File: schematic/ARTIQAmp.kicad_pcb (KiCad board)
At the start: 2 copper layers, 297 parts, among them J1 Power conneciton, J2 HD68, J3 HD68, U1 OPA454AIDDAR, U10 OPA454AIDDAR, U11 OPA454AIDDAR, U12 OPA454AIDDAR, U13 OPA454AIDDAR, U14 OPA454AIDDAR, U15 OPA454AIDDAR, U16 OPA454AIDDAR, U17 OPA454AIDDAR, U18 OPA454AIDDAR, U19 OPA454AIDDAR, U2 OPA454AIDDAR, U20 OPA454AIDDAR, U21 OPA454AIDDAR, U22 OPA454AIDDAR, U23 OPA454AIDDAR, U24 OPA454AIDDAR, U25 OPA454AIDDAR, U26 OPA454AIDDAR, U27 OPA454AIDDAR, U28 OPA454AIDDAR, U29 OPA454AIDDAR, U3 OPA454AIDDAR, U30 OPA454AIDDAR, U31 OPA454AIDDAR, U32 OPA454AIDDAR, U4 OPA454AIDDAR, U5 OPA454AIDDAR, U6 OPA454AIDDAR, U7 OPA454AIDDAR, U8 OPA454AIDDAR, U9 OPA454AIDDAR

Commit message: Update libraries for new components
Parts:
- added FL1: NFE61PT472C1H9L, ARTIQAmp:NFE61, F.Cu at (178.5, 211.5)
- added FL10: NFE61PT472C1H9L, ARTIQAmp:NFE61, F.Cu at (261.0, 182.2)
- added FL11: NFE61PT472C1H9L, ARTIQAmp:NFE61, F.Cu at (223.8, 182.2)
- added FL12: NFE61PT472C1H9L, ARTIQAmp:NFE61, F.Cu at (207.6, 36.6)
- added FL13: NFE61PT472C1H9L, ARTIQAmp:NFE61, F.Cu at (243.5, 182.2)
- added FL14: NFE61PT472C1H9L, ARTIQAmp:NFE61, F.Cu at (368.3, 129.3)
- added FL15: NFE61PT472C1H9L, ARTIQAmp:NFE61, F.Cu at (279.5, 182.5)
- added FL16: NFE61PT472C1H9L, ARTIQAmp:NFE61, F.Cu at (207.6, 26.2)
- added FL17: NFE61PT472C1H9L, ARTIQAmp:NFE61, B.Cu at (163.8, 249.8)
- added FL18: NFE61PT472C1H9L, ARTIQAmp:NFE61, B.Cu at (183.5, 249.0)
- added FL19: NFE61PT472C1H9L, ARTIQAmp:NFE61, B.Cu at (125.8, 250.0)
- added FL2: NFE61PT472C1H9L, ARTIQAmp:NFE61, F.Cu at (379.3, 102.3)
- added FL20: NFE61PT472C1H9L, ARTIQAmp:NFE61, F.Cu at (-0.35, 228.0)
- added FL21: NFE61PT472C1H9L, ARTIQAmp:NFE61, B.Cu at (201.0, 249.0)
- added FL22: NFE61PT472C1H9L, ARTIQAmp:NFE61, F.Cu at (428.8, 215.2)
- added FL23: NFE61PT472C1H9L, ARTIQAmp:NFE61, F.Cu at (57.2, 105.2)
- added FL24: NFE61PT472C1H9L, ARTIQAmp:NFE61, B.Cu at (143.2, 250.0)
- added FL25: NFE61PT472C1H9L, ARTIQAmp:NFE61, F.Cu at (127.0, 145.8)
- added FL26: NFE61PT472C1H9L, ARTIQAmp:NFE61, F.Cu at (180.2, 181.5)
- added FL27: NFE61PT472C1H9L, ARTIQAmp:NFE61, F.Cu at (-0.35, 207.2)
- added FL28: NFE61PT472C1H9L, ARTIQAmp:NFE61, F.Cu at (200.2, 181.0)
- added FL29: NFE61PT472C1H9L, ARTIQAmp:NFE61, F.Cu at (162.8, 181.5)
- added FL3: NFE61PT472C1H9L, ARTIQAmp:NFE61, F.Cu at (220.1, 2.58)
- added FL30: NFE61PT472C1H9L, ARTIQAmp:NFE61, F.Cu at (-0.35, 196.8)
- added FL31: NFE61PT472C1H9L, ARTIQAmp:NFE61, F.Cu at (267.2, 145.8)
- added FL32: NFE61PT472C1H9L, ARTIQAmp:NFE61, F.Cu at (-0.35, 186.4)
- added FL4: NFE61PT472C1H9L, ARTIQAmp:NFE61, F.Cu at (161.0, 211.5)
- added FL5: NFE61PT472C1H9L, ARTIQAmp:NFE61, F.Cu at (408.4, 261.0)
- added FL6: NFE61PT472C1H9L, ARTIQAmp:NFE61, F.Cu at (143.5, 211.5)
- added FL7: NFE61PT472C1H9L, ARTIQAmp:NFE61, F.Cu at (207.6, 47.0)
- added FL8: NFE61PT472C1H9L, ARTIQAmp:NFE61, F.Cu at (284.1, 31.6)
- added FL9: NFE61PT472C1H9L, ARTIQAmp:NFE61, F.Cu at (220.1, -7.83)
- C100, C72, C76, C80, C88: value 0.27uF -> 5nF; moved to B.Cu
- C101, C73, C77, C81, C89: value 1.3nF -> 160p; moved to B.Cu
- C102, C71, C74, C75, C78, C79, C82, C87, C90, C99, R65, R67, R68, R69, R71, R72, R73, R75, R76, R81, R83, R84, R93, R95, R96, U17, U18, U19, U21, U24: moved to B.Cu
- C104, C108, C112, C116, C12, C120, C124, C128, C132, C16, C20, C24, C28, C32, C36, C40, C44, C48, C52, C56, C60, C64, C68, C8, C84, C92, C96: value 0.27uF -> 5nF
- C105, C109, C113, C117, C121, C125, C129, C13, C133, C17, C21, C25, C29, C33, C37, C41, C45, C49, C53, C57, C61, C65, C69, C85, C9, C93, C97: value 1.3nF -> 160p
- R10, R102, R106, R110, R114, R118, R122, R126, R14, R18, R2, R22, R26, R30, R34, R38, R42, R46, R50, R54, R58, R6, R62, R78, R86, R90, R98: value 49R9 -> 30R
- R66, R70, R74, R82, R94: value 49R9 -> 30R; moved to B.Cu
- moved C112 337.2 mm to (425.8, 201.6)
- moved C114 337.2 mm to (429.8, 201.6)
- moved C127 337.2 mm to (449.9, 201.6)
- moved C129 337.2 mm to (445.9, 201.6)
- moved C130 337.2 mm to (457.9, 200.0)
- moved C84 337.2 mm to (413.7, 188.9)
- moved C85 337.2 mm to (417.7, 187.4)
- moved C91 337.2 mm to (437.8, 187.4)
- moved C92 337.2 mm to (438.3, 184.9)
- moved C93 337.2 mm to (433.8, 188.9)
- moved C94 337.2 mm to (438.3, 182.4)
- moved C96 337.2 mm to (413.7, 201.6)
- moved C97 337.2 mm to (417.7, 200.0)
- moved R105 337.2 mm to (438.3, 195.0)
- moved R106 337.2 mm to (433.8, 201.6)
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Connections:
- R10 pad 2: /D4_IN -> Net-(FL3-Pad2)
- R102 pad 2: /D27_IN -> Net-(FL26-Pad2)
- R106 pad 2: /D28_IN -> Net-(FL27-Pad2)
- R110 pad 2: /D29_IN -> Net-(FL28-Pad2)
- R114 pad 2: /D30_IN -> Net-(FL29-Pad2)
- R118 pad 2: /D31_IN -> Net-(FL30-Pad2)
- R122 pad 2: /D32_IN -> Net-(FL31-Pad2)
- R126 pad 2: /D25_IN -> Net-(FL32-Pad2)
- R14 pad 2: /D5_IN -> Net-(FL4-Pad2)
- R18 pad 2: /D6_IN -> Net-(FL5-Pad2)
- R2 pad 2: /D2_IN -> Net-(FL1-Pad2)
- R22 pad 2: /D7_IN -> Net-(FL6-Pad2)
- R26 pad 2: /D8_IN -> Net-(FL7-Pad2)
- R30 pad 2: /D1_IN -> Net-(FL8-Pad2)
- R34 pad 2: /D10_IN -> Net-(FL9-Pad2)
- R38 pad 2: /D11_IN -> Net-(FL10-Pad2)
- R42 pad 2: /D12_IN -> Net-(FL11-Pad2)
- R46 pad 2: /D13_IN -> Net-(FL12-Pad2)
- R50 pad 2: /D14_IN -> Net-(FL13-Pad2)
- R54 pad 2: /D15_IN -> Net-(FL14-Pad2)
- R58 pad 2: /D16_IN -> Net-(FL15-Pad2)
- R6 pad 2: /D3_IN -> Net-(FL2-Pad2)
- R62 pad 2: /D9_IN -> Net-(FL16-Pad2)
- R66 pad 2: /D18_IN -> Net-(FL17-Pad2)
- R70 pad 2: /D19_IN -> Net-(FL18-Pad2)
- R74 pad 2: /D20_IN -> Net-(FL19-Pad2)
- R78 pad 2: /D21_IN -> Net-(FL20-Pad2)
- R82 pad 2: /D22_IN -> Net-(FL21-Pad2)
- R86 pad 2: /D23_IN -> Net-(FL22-Pad2)
- R90 pad 2: /D24_IN -> Net-(FL23-Pad2)
- R94 pad 2: /D17_IN -> Net-(FL24-Pad2)
- R98 pad 2: /D26_IN -> Net-(FL25-Pad2)
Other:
- board outline added: 380 x 160 mm
- copper layers 2 -> 8

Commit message: finalize schematic and start organizing components in layout
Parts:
- removed the C100 at (147.0, 256.2)
- removed the C101 at (149.8, 263.5)
- removed the C102 at (153.5, 254.2)
- removed C103, C106, C119, C122, C123: 0.1uF, Capacitor_SMD:C_0603_1608Metric
- removed C104, C120: 5nF, Capacitor_SMD:C_0603_1608Metric
- removed C105, C109, C113, C117, C121, C125, C129, C133: 160p, Capacitor_SMD:C_0603_1608Metric
- removed the C13 at (464.0, 239.1)
- removed the C17 at (471.8, 180.0)
- removed the C21 at (167.5, 198.0)
- removed the C25 at (443.2, 268.8)
- removed the C27 at (156.8, 204.2)
- removed the C33 at (471.8, 167.3)
- removed the C35 at (466.4, 261.9)
- removed the C36 at (461.8, 265.9)
- removed the C37 at (466.4, 259.4)
- removed the C38 at (470.4, 259.4)
- removed the C41 at (385.9, 184.8)
- removed the C45 at (267.5, 168.8)
- removed the C49 at (230.2, 168.8)
- removed the C53 at (471.3, 157.2)
- removed the C65 at (286.0, 169.0)
- removed the C71 at (177.0, 257.0)
- removed the C72 at (167.5, 256.0)
- removed the C73 at (170.2, 263.2)
- removed the C74 at (174.0, 254.0)
- removed the C75 at (196.8, 256.2)
- removed the C82 at (136.0, 254.2)
- removed the C85 at (417.7, 187.4)
- removed the C87 at (214.2, 256.2)
- removed the C88 at (204.8, 255.2)
- removed the C89 at (207.5, 262.5)
- removed the C9 at (185.0, 198.0)
- removed the C90 at (211.2, 253.2)
- removed the C97 at (417.7, 200.0)
- removed the C99 at (156.5, 257.2)
- removed the R116 at (165.2, 172.8)
- removed the R17 at (430.7, 272.8)
- removed the R23 at (150.0, 199.8)
- removed the R24 at (146.0, 202.8)
- removed the R29 at (457.8, 265.9)
- removed the R30 at (465.8, 265.9)
- removed the R41 at (236.0, 170.5)
- removed the R5 at (460.0, 236.6)
- removed the R53 at (389.9, 172.1)
- removed the R65 at (176.0, 261.5)
- removed the R66 at (165.0, 256.8)
- removed the R68 at (166.2, 258.5)
- removed the R71 at (190.0, 260.8)
- removed the R72 at (186.0, 257.8)
- removed the R74 at (127.0, 257.0)
- removed the R83 at (207.5, 260.8)
- removed the R84 at (203.5, 257.8)
- removed the R89 at (405.7, 201.6)
- removed the R95 at (149.8, 261.8)
- removed the R96 at (145.8, 258.8)
- removed U1, U10, U11, U12, U13, U14, U15, U16, U17, U18, U19, U2, U20, U21, U22, U23, U24, U25, U26, U27, U28, U29, U3, U30, U31, U32, U4, U5, U6, U7, U8, U9: OPA454AIDDAR, ARTIQAmp:TI_SO-PowerPAD-8_ThermalVias
- added C22: 0.1uF, Capacitor_SMD:C_0603_1608Metric, F.Cu at (224.8, 157.8)
- added C23: 1nF, Capacitor_SMD:C_0603_1608Metric, F.Cu at (215.6, 160.2)
- added C24: 0.1uF, Capacitor_SMD:C_0603_1608Metric, F.Cu at (222.4, 160.8)
- added C43: 0.1uF, Capacitor_SMD:C_0603_1608Metric, F.Cu at (224.8, 134.8)
- added C56: 1nF, Capacitor_SMD:C_0603_1608Metric, F.Cu at (153.5, 160.2)
- added C58: 0.1uF, Capacitor_SMD:C_0603_1608Metric, F.Cu at (183.4, 157.8)
- added C59: 1nF, Capacitor_SMD:C_0603_1608Metric, F.Cu at (174.2, 160.2)
- added C60: 0.1uF, Capacitor_SMD:C_0603_1608Metric, F.Cu at (181.0, 160.8)
- added C62: 1nF, Capacitor_SMD:C_0603_1608Metric, F.Cu at (112.1, 160.2)
- added C63: 0.1uF, Capacitor_SMD:C_0603_1608Metric, F.Cu at (118.9, 160.8)
- added C67: 0.1uF, Capacitor_SMD:C_0603_1608Metric, F.Cu at (204.1, 157.8)
- added C68: 1nF, Capacitor_SMD:C_0603_1608Metric, F.Cu at (194.9, 160.2)
- added C91: 0.1uF, Capacitor_SMD:C_0603_1608Metric, F.Cu at (142.0, 134.8)
- added C92: 1nF, Capacitor_SMD:C_0603_1608Metric, F.Cu at (132.8, 137.2)
- added C94: 0.1uF, Capacitor_SMD:C_0603_1608Metric, F.Cu at (286.9, 157.8)
- added IC1: LTC6090CS8E#PBF, ARTIQAmp:SOIC127P599X175-9N, F.Cu at (261.6, 157.2)
- added IC10: LTC6090CS8E#PBF, ARTIQAmp:SOIC127P599X175-9N, F.Cu at (240.9, 134.2)
- added IC11: LTC6090CS8E#PBF, ARTIQAmp:SOIC127P599X175-9N, F.Cu at (199.5, 134.2)
- added IC12: LTC6090CS8E#PBF, ARTIQAmp:SOIC127P599X175-9N, F.Cu at (344.4, 134.2)
- added IC13: LTC6090CS8E#PBF, ARTIQAmp:SOIC127P599X175-9N, F.Cu at (220.2, 134.2)
- added IC14: LTC6090CS8E#PBF, ARTIQAmp:SOIC127P599X175-9N, F.Cu at (303.0, 134.2)
- added IC15: LTC6090CS8E#PBF, ARTIQAmp:SOIC127P599X175-9N, F.Cu at (261.6, 134.2)
- added IC16: LTC6090CS8E#PBF, ARTIQAmp:SOIC127P599X175-9N, F.Cu at (323.7, 157.2)
- added IC17: LTC6090CS8E#PBF, ARTIQAmp:SOIC127P599X175-9N, F.Cu at (158.1, 157.2)
- added IC18: LTC6090CS8E#PBF, ARTIQAmp:SOIC127P599X175-9N, F.Cu at (178.8, 157.2)
- added IC19: LTC6090CS8E#PBF, ARTIQAmp:SOIC127P599X175-9N, F.Cu at (116.7, 157.2)
- added IC2: LTC6090CS8E#PBF, ARTIQAmp:SOIC127P599X175-9N, F.Cu at (365.1, 134.2)
- added IC20: LTC6090CS8E#PBF, ARTIQAmp:SOIC127P599X175-9N, F.Cu at (365.1, 157.2)
- added IC21: LTC6090CS8E#PBF, ARTIQAmp:SOIC127P599X175-9N, F.Cu at (199.5, 157.2)
- added IC22: LTC6090CS8E#PBF, ARTIQAmp:SOIC127P599X175-9N, F.Cu at (323.7, 134.2)
- added IC23: LTC6090CS8E#PBF, ARTIQAmp:SOIC127P599X175-9N, F.Cu at (385.8, 157.2)
- added IC24: LTC6090CS8E#PBF, ARTIQAmp:SOIC127P599X175-9N, F.Cu at (137.4, 157.2)
- added IC25: LTC6090CS8E#PBF, ARTIQAmp:SOIC127P599X175-9N, F.Cu at (116.7, 134.2)
- added IC26: LTC6090CS8E#PBF, ARTIQAmp:SOIC127P599X175-9N, F.Cu at (158.1, 134.2)
- added IC27: LTC6090CS8E#PBF, ARTIQAmp:SOIC127P599X175-9N, F.Cu at (385.8, 134.2)
- added IC28: LTC6090CS8E#PBF, ARTIQAmp:SOIC127P599X175-9N, F.Cu at (178.8, 134.2)
- added IC29: LTC6090CS8E#PBF, ARTIQAmp:SOIC127P599X175-9N, F.Cu at (137.4, 134.2)
- added IC3: LTC6090CS8E#PBF, ARTIQAmp:SOIC127P599X175-9N, F.Cu at (406.5, 134.2)
- added IC30: LTC6090CS8E#PBF, ARTIQAmp:SOIC127P599X175-9N, F.Cu at (282.3, 157.2)
- added IC31: LTC6090CS8E#PBF, ARTIQAmp:SOIC127P599X175-9N, F.Cu at (427.2, 157.2)
- added IC32: LTC6090CS8E#PBF, ARTIQAmp:SOIC127P599X175-9N, F.Cu at (406.5, 157.2)
- added IC4: LTC6090CS8E#PBF, ARTIQAmp:SOIC127P599X175-9N, F.Cu at (240.9, 157.2)
- added IC5: LTC6090CS8E#PBF, ARTIQAmp:SOIC127P599X175-9N, F.Cu at (344.4, 157.2)
- added IC6: LTC6090CS8E#PBF, ARTIQAmp:SOIC127P599X175-9N, F.Cu at (220.2, 157.2)
- added IC7: LTC6090CS8E#PBF, ARTIQAmp:SOIC127P599X175-9N, F.Cu at (303.0, 157.2)
- added IC8: LTC6090CS8E#PBF, ARTIQAmp:SOIC127P599X175-9N, F.Cu at (427.2, 134.2)
- added IC9: LTC6090CS8E#PBF, ARTIQAmp:SOIC127P599X175-9N, F.Cu at (282.3, 134.2)
- added L1: 744229, ARTIQAmp:WE-SL2, F.Cu at (267.9, 166.7)
- added L10: 744229, ARTIQAmp:WE-SL2, F.Cu at (247.2, 143.7)
- added L11: 744229, ARTIQAmp:WE-SL2, F.Cu at (205.8, 143.7)
- added L12: 744229, ARTIQAmp:WE-SL2, F.Cu at (350.7, 143.7)
- added L13: 744229, ARTIQAmp:WE-SL2, F.Cu at (226.5, 143.7)
- added L14: 744229, ARTIQAmp:WE-SL2, F.Cu at (309.3, 143.7)
- added L15: 744229, ARTIQAmp:WE-SL2, F.Cu at (267.9, 143.7)
- added L16: 744229, ARTIQAmp:WE-SL2, F.Cu at (330.0, 166.7)
- added L17: 744229, ARTIQAmp:WE-SL2, F.Cu at (164.4, 166.7)
- added L18: 744229, ARTIQAmp:WE-SL2, F.Cu at (185.1, 166.7)
- added L19: 744229, ARTIQAmp:WE-SL2, F.Cu at (123.0, 166.7)
- added L2: 744229, ARTIQAmp:WE-SL2, F.Cu at (371.4, 143.7)
- added L20: 744229, ARTIQAmp:WE-SL2, F.Cu at (371.4, 166.7)
- added L21: 744229, ARTIQAmp:WE-SL2, F.Cu at (205.8, 166.7)
- added L22: 744229, ARTIQAmp:WE-SL2, F.Cu at (330.0, 143.7)
- added L23: 744229, ARTIQAmp:WE-SL2, F.Cu at (392.1, 166.7)
- added L24: 744229, ARTIQAmp:WE-SL2, F.Cu at (143.7, 166.7)
- added L25: 744229, ARTIQAmp:WE-SL2, F.Cu at (123.0, 143.7)
- added L26: 744229, ARTIQAmp:WE-SL2, F.Cu at (164.4, 143.7)
- added L27: 744229, ARTIQAmp:WE-SL2, F.Cu at (392.1, 143.7)
- added L28: 744229, ARTIQAmp:WE-SL2, F.Cu at (185.1, 143.7)
- added L29: 744229, ARTIQAmp:WE-SL2, F.Cu at (143.7, 143.7)
- added L3: 744229, ARTIQAmp:WE-SL2, F.Cu at (412.8, 143.7)
- added L30: 744229, ARTIQAmp:WE-SL2, F.Cu at (288.6, 166.7)
- added L31: 744229, ARTIQAmp:WE-SL2, F.Cu at (433.5, 166.7)
- added L32: 744229, ARTIQAmp:WE-SL2, F.Cu at (412.8, 166.7)
- added L4: 744229, ARTIQAmp:WE-SL2, F.Cu at (247.2, 166.7)
- added L5: 744229, ARTIQAmp:WE-SL2, F.Cu at (350.7, 166.7)
- added L6: 744229, ARTIQAmp:WE-SL2, F.Cu at (226.5, 166.7)
- added L7: 744229, ARTIQAmp:WE-SL2, F.Cu at (309.3, 166.7)
- added L8: 744229, ARTIQAmp:WE-SL2, F.Cu at (433.5, 143.7)
- added L9: 744229, ARTIQAmp:WE-SL2, F.Cu at (288.6, 143.7)
- added R10: 30R, Resistor_SMD:R_0603_1608Metric, F.Cu at (371.3, 135.7)
- added R102: 1.65k, Resistor_SMD:R_0603_1608Metric, F.Cu at (151.1, 156.6)
- added R103: 0R, Resistor_SMD:R_0603_1608Metric, F.Cu at (174.2, 168.9)
- added R104: 100R, Resistor_SMD:R_0603_1608Metric, F.Cu at (171.8, 158.2)
- added R106: 30R, Resistor_SMD:R_0603_1608Metric, F.Cu at (185.0, 158.7)
- added R107: 4.99k, Resistor_SMD:R_0603_1608Metric, F.Cu at (178.8, 153.6)
- added R108: 1.65k, Resistor_SMD:R_0603_1608Metric, F.Cu at (171.8, 156.6)
- added R110: 100R, Resistor_SMD:R_0603_1608Metric, F.Cu at (109.7, 158.2)
- added R111: 4.99k, Resistor_SMD:R_0603_1608Metric, F.Cu at (112.1, 157.2)
- added R112: 30R, Resistor_SMD:R_0603_1608Metric, F.Cu at (122.9, 158.7)
- added R118: 30R, Resistor_SMD:R_0603_1608Metric, F.Cu at (371.3, 158.7)
- added R122: 100R, Resistor_SMD:R_0603_1608Metric, F.Cu at (192.5, 158.2)
- added R123: 4.99k, Resistor_SMD:R_0603_1608Metric, F.Cu at (194.9, 157.2)
- added R124: 30R, Resistor_SMD:R_0603_1608Metric, F.Cu at (205.7, 158.7)
- added R126: 1.65k, Resistor_SMD:R_0603_1608Metric, F.Cu at (192.5, 156.6)
- added R127: 0R, Resistor_SMD:R_0603_1608Metric, F.Cu at (319.1, 145.9)
- added R129: 4.99k, Resistor_SMD:R_0603_1608Metric, F.Cu at (319.1, 134.2)
- added R130: 30R, Resistor_SMD:R_0603_1608Metric, F.Cu at (329.9, 135.7)
- added R133: 0R, Resistor_SMD:R_0603_1608Metric, F.Cu at (381.2, 168.9)
- added R135: 4.99k, Resistor_SMD:R_0603_1608Metric, F.Cu at (381.2, 157.2)
- added R136: 30R, Resistor_SMD:R_0603_1608Metric, F.Cu at (392.0, 158.7)
- added R139: 0R, Resistor_SMD:R_0603_1608Metric, F.Cu at (132.8, 168.9)
- added R140: 100R, Resistor_SMD:R_0603_1608Metric, F.Cu at (130.4, 158.2)
- added R141: 4.99k, Resistor_SMD:R_0603_1608Metric, F.Cu at (132.8, 157.2)
- added R142: 30R, Resistor_SMD:R_0603_1608Metric, F.Cu at (143.6, 158.7)
- added R143: 4.99k, Resistor_SMD:R_0603_1608Metric, F.Cu at (137.4, 153.6)
- added R144: 1.65k, Resistor_SMD:R_0603_1608Metric, F.Cu at (130.4, 156.6)
- added R145: 0R, Resistor_SMD:R_0603_1608Metric, F.Cu at (112.1, 145.9)
- added R146: 100R, Resistor_SMD:R_0603_1608Metric, F.Cu at (109.7, 135.2)
- added R147: 4.99k, Resistor_SMD:R_0603_1608Metric, F.Cu at (112.1, 134.2)
- added R148: 30R, Resistor_SMD:R_0603_1608Metric, F.Cu at (122.9, 135.7)
- added R149: 4.99k, Resistor_SMD:R_0603_1608Metric, F.Cu at (116.7, 130.6)
- added R15: 4.99k, Resistor_SMD:R_0603_1608Metric, F.Cu at (401.9, 134.2)
- added R150: 1.65k, Resistor_SMD:R_0603_1608Metric, F.Cu at (109.7, 133.6)
- added R151: 0R, Resistor_SMD:R_0603_1608Metric, F.Cu at (153.5, 145.9)
- added R153: 4.99k, Resistor_SMD:R_0603_1608Metric, F.Cu at (153.5, 134.2)
- added R154: 30R, Resistor_SMD:R_0603_1608Metric, F.Cu at (164.3, 135.7)
- added R157: 0R, Resistor_SMD:R_0603_1608Metric, F.Cu at (381.2, 145.9)
- added R159: 4.99k, Resistor_SMD:R_0603_1608Metric, F.Cu at (381.2, 134.2)
- added R16: 30R, Resistor_SMD:R_0603_1608Metric, F.Cu at (412.7, 135.7)
- added R160: 30R, Resistor_SMD:R_0603_1608Metric, F.Cu at (392.0, 135.7)
- added R163: 0R, Resistor_SMD:R_0603_1608Metric, F.Cu at (174.2, 145.9)
- added R165: 4.99k, Resistor_SMD:R_0603_1608Metric, F.Cu at (174.2, 134.2)
- added R166: 30R, Resistor_SMD:R_0603_1608Metric, F.Cu at (185.0, 135.7)
- added R169: 0R, Resistor_SMD:R_0603_1608Metric, F.Cu at (132.8, 145.9)
- added R170: 100R, Resistor_SMD:R_0603_1608Metric, F.Cu at (130.4, 135.2)
- added R171: 4.99k, Resistor_SMD:R_0603_1608Metric, F.Cu at (132.8, 134.2)
- added R172: 30R, Resistor_SMD:R_0603_1608Metric, F.Cu at (143.6, 135.7)
- added R173: 4.99k, Resistor_SMD:R_0603_1608Metric, F.Cu at (137.4, 130.4)
- added R174: 1.65k, Resistor_SMD:R_0603_1608Metric, F.Cu at (130.4, 133.6)
- added R175: 0R, Resistor_SMD:R_0603_1608Metric, F.Cu at (277.7, 168.9)
- added R177: 4.99k, Resistor_SMD:R_0603_1608Metric, F.Cu at (277.7, 157.2)
- added R178: 30R, Resistor_SMD:R_0603_1608Metric, F.Cu at (288.5, 158.7)
- added R181: 0R, Resistor_SMD:R_0603_1608Metric, F.Cu at (422.6, 168.9)
- added R183: 4.99k, Resistor_SMD:R_0603_1608Metric, F.Cu at (422.6, 157.2)
- added R184: 30R, Resistor_SMD:R_0603_1608Metric, F.Cu at (433.4, 158.7)
- added R187: 0R, Resistor_SMD:R_0603_1608Metric, F.Cu at (401.9, 168.9)
- added R189: 4.99k, Resistor_SMD:R_0603_1608Metric, F.Cu at (401.9, 157.2)
- added R19: 0R, Resistor_SMD:R_0603_1608Metric, F.Cu at (236.3, 168.9)
- added R190: 30R, Resistor_SMD:R_0603_1608Metric, F.Cu at (412.7, 158.7)
- added R27: 4.99k, Resistor_SMD:R_0603_1608Metric, F.Cu at (339.8, 157.2)
- added R28: 30R, Resistor_SMD:R_0603_1608Metric, F.Cu at (350.6, 158.7)
- added R3: 4.99k, Resistor_SMD:R_0603_1608Metric, F.Cu at (257.0, 157.2)
- added R34: 30R, Resistor_SMD:R_0603_1608Metric, F.Cu at (226.4, 158.7)
- added R35: 4.99k, Resistor_SMD:R_0603_1608Metric, F.Cu at (220.2, 153.6)
- added R36: 1.65k, Resistor_SMD:R_0603_1608Metric, F.Cu at (213.2, 156.6)
- added R39: 4.99k, Resistor_SMD:R_0603_1608Metric, F.Cu at (298.4, 157.2)
- added R4: 30R, Resistor_SMD:R_0603_1608Metric, F.Cu at (267.8, 158.7)
- added R40: 30R, Resistor_SMD:R_0603_1608Metric, F.Cu at (309.2, 158.7)
- added R43: 0R, Resistor_SMD:R_0603_1608Metric, F.Cu at (422.6, 145.9)
- added R44: 100R, Resistor_SMD:R_0603_1608Metric, F.Cu at (420.2, 135.2)
- added R46: 30R, Resistor_SMD:R_0603_1608Metric, F.Cu at (433.4, 135.7)
- added R47: 4.99k, Resistor_SMD:R_0603_1608Metric, F.Cu at (427.2, 130.6)
- added R48: 1.65k, Resistor_SMD:R_0603_1608Metric, F.Cu at (420.2, 133.6)
- added R52: 30R, Resistor_SMD:R_0603_1608Metric, F.Cu at (288.5, 135.7)
- added R55: 0R, Resistor_SMD:R_0603_1608Metric, F.Cu at (236.3, 145.9)
- added R58: 30R, Resistor_SMD:R_0603_1608Metric, F.Cu at (247.1, 135.7)
- added R63: 4.99k, Resistor_SMD:R_0603_1608Metric, F.Cu at (194.9, 134.2)
- added R64: 30R, Resistor_SMD:R_0603_1608Metric, F.Cu at (205.7, 135.7)
- added R7: 0R, Resistor_SMD:R_0603_1608Metric, F.Cu at (360.5, 146.7)
- added R79: 0R, Resistor_SMD:R_0603_1608Metric, F.Cu at (298.4, 145.9)
- added R87: 4.99k, Resistor_SMD:R_0603_1608Metric, F.Cu at (257.0, 134.2)
- added R88: 30R, Resistor_SMD:R_0603_1608Metric, F.Cu at (267.8, 135.7)
- added R91: 0R, Resistor_SMD:R_0603_1608Metric, F.Cu at (319.1, 168.9)
- C101: renamed from C132; value 5nF -> 1nF
- C11: renamed from C12; value 5nF -> 1nF
- C14: renamed from C16; value 5nF -> 1nF
- C17: renamed from C20; value 5nF -> 1nF
- C20: renamed from C24; value 5nF -> 1nF
- C26: renamed from C32; value 5nF -> 1nF
- C28: value 5nF -> 0.1uF
- C29: value 160p -> 1nF
- C32: renamed from C40; value 5nF -> 1nF
- C35: renamed from C44; value 5nF -> 1nF
- C38: renamed from C48; value 5nF -> 1nF
- C41: renamed from C52; value 5nF -> 1nF
- C44: renamed from C56; value 5nF -> 1nF
- C47: renamed from C60; value 5nF -> 1nF
- C50: renamed from C64; value 5nF -> 1nF
- C53: renamed from C68; value 5nF -> 1nF
- C57, C61, C69, C93: value 160p -> 0.1uF
- C65: renamed from C84; value 5nF -> 1nF
- C71: renamed from C92; value 5nF -> 1nF
- C74: renamed from C96; value 5nF -> 1nF
- C76: value 5nF -> 0.1uF; moved to F.Cu
- C77: value 160p -> 1nF; moved to F.Cu
- C78, C79, FL17, FL18, FL19, FL21, FL24, R70, R75, R82, R94: moved to F.Cu
- C8: value 5nF -> 1nF
- C80: value 5nF -> 1nF; moved to F.Cu
- C81: value 160p -> 0.1uF; moved to F.Cu
- C83: renamed from C108; value 5nF -> 1nF
- C86: renamed from C112; value 5nF -> 1nF
- C89: renamed from C116; value 5nF -> 1nF
- C95: renamed from C124; value 5nF -> 1nF
- C98: renamed from C128; value 5nF -> 1nF
- R1, R109, R121, R13, R25, R37, R49, R61, R85, R97: value 1M -> 0R
- R100: value 1.65k -> 30R
- R101, R105, R113, R117, R125, R21, R33, R45, R57, R77, R9: value 1M -> 4.99k
- R114: value 30R -> 1.65k
- R115, R31: value 4.99k -> 0R
- R116: renamed from R78; value 30R -> 100R
- R128: renamed from R86; value 30R -> 100R
- R134: renamed from R90; value 30R -> 100R
- R14: renamed from R10; value 30R -> 100R
- R152: renamed from R102; value 30R -> 100R
- R158: renamed from R106; value 30R -> 100R
- R164: renamed from R110; value 30R -> 100R
- R176: renamed from R118; value 30R -> 100R
- R182: renamed from R122; value 30R -> 100R
- R188: renamed from R126; value 30R -> 100R
- R2, R98: value 30R -> 100R
- R20: renamed from R14; value 30R -> 100R
- R26: renamed from R18; value 30R -> 100R
- R32: value 1.65k -> 100R
- R38: renamed from R26; value 30R -> 100R
- R50: renamed from R34; value 30R -> 100R
- R56: renamed from R38; value 30R -> 100R
- R62: renamed from R42; value 30R -> 100R
- R67: value 4.99k -> 0R; moved to F.Cu
- R68: renamed from R46; value 30R -> 100R
- R69, R81, R93: value 1M -> 4.99k; moved to F.Cu
- R73: value 1M -> 0R; moved to F.Cu
- R74: renamed from R50; value 30R -> 100R
- R76: value 1.65k -> 30R; moved to F.Cu
- R8: renamed from R6; value 30R -> 100R
- R80: renamed from R54; value 30R -> 100R
- R86: renamed from R58; value 30R -> 100R
- R92: renamed from R62; value 30R -> 100R
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- renumbered C11 to C10, C131 to C100, C134 to C102, C14 to C12, C15 to C13, C18 to C15, C19 to C16, C22 to C18, C23 to C19, C26 to C21, C31 to C25, C34 to C27, C39 to C31, C42 to C33, C43 to C34, C46 to C36, C47 to C37, C50 to C39, C51 to C40, C54 to C42, C58 to C45, C59 to C46, C62 to C48, C63 to C49, C66 to C51, C67 to C52, C70 to C54, C83 to C64, C86 to C66, C91 to C70, C94 to C72, C95 to C73, C98 to C75, C107 to C82, C110 to C84, C111 to C85, C114 to C87, C115 to C88, C10 to C9, C118 to C90, C126 to C96, C127 to C97, C130 to C99, R7 to R11, R79 to R119, R8 to R12, R80 to R120, R87 to R131, R88 to R132, R91 to R137, R92 to R138, R103 to R155, R104 to R156, R107 to R161, R108 to R162, R111 to R167, R112 to R168, R11 to R17, R119 to R179, R12 to R18, R120 to R180, R123 to R185, R124 to R186, R127 to R191, R128 to R192, R15 to R23, R16 to R24, R19 to R29, R20 to R30, R27 to R41, R28 to R42, R3 to R5, R35 to R53, R36 to R54, R39 to R59, R4 to R6, R40 to R60, R43 to R65, R44 to R66, R47 to R71, R48 to R72, R52 to R78, R55 to R83, R56 to R84, R59 to R89, R60 to R90, R63 to R95, R64 to R96
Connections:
- C10 pad 1: /D3_HV_OUT_COM -> /D3_IN_COM
- C100 pad 1: /D25_HV_OUT_COM -> /D25_IN_COM
- C101 pad 2: /D25_HV_OUT_COM -> /D25_IN_COM
- C102 pad 1: /D25_HV_OUT_COM -> /D25_IN_COM
- C11 pad 1: Net-(C12-Pad1) -> Net-(C11-Pad1)
- C11 pad 2: /D3_HV_OUT_COM -> /D3_IN_COM
- C12 pad 1: /D3_HV_OUT_COM -> /D3_IN_COM
- C13 pad 1: /D4_HV_OUT_COM -> /D4_IN_COM
- C14 pad 2: /D4_HV_OUT_COM -> /D4_IN_COM
- C15 pad 1: /D4_HV_OUT_COM -> /D4_IN_COM
- C16 pad 1: /D5_HV_OUT_COM -> /D5_IN_COM
- C17 pad 1: Net-(C20-Pad1) (its old number) -> Net-(C17-Pad1)
- C17 pad 2: /D5_HV_OUT_COM -> /D5_IN_COM
- C18 pad 1: /D5_HV_OUT_COM -> /D5_IN_COM
- C19 pad 1: /D6_HV_OUT_COM -> /D6_IN_COM
- C20 pad 2: /D6_HV_OUT_COM -> /D6_IN_COM
- C21 pad 1: /D6_HV_OUT_COM -> /D6_IN_COM
- C25 pad 1: /D8_HV_OUT_COM -> /D8_IN_COM
- C26 pad 2: /D8_HV_OUT_COM -> /D8_IN_COM
- C27 pad 1: /D8_HV_OUT_COM -> /D8_IN_COM
- C28 pad 1: Net-(C28-Pad1) -> /D1_IN_COM
- C28 pad 2: /D7_HV_OUT_COM -> +48V
- C29 pad 1: /D7_HV_OUT -> Net-(C29-Pad1)
- C29 pad 2: Net-(C29-Pad2) -> /D1_IN_COM
- C30 pad 1: /D7_HV_OUT_COM -> /D1_IN_COM
- C31 pad 1: /D10_HV_OUT_COM -> /D10_IN_COM
- C32 pad 1: Net-(C40-Pad1) -> Net-(C32-Pad1)
- C32 pad 2: /D10_HV_OUT_COM -> /D10_IN_COM
- C33 pad 1: /D10_HV_OUT_COM -> /D10_IN_COM
- C34 pad 1: /D11_HV_OUT_COM -> /D11_IN_COM
- C35 pad 1: Net-(C44-Pad1) -> Net-(C35-Pad1)
- C35 pad 2: /D11_HV_OUT_COM -> /D11_IN_COM
- C36 pad 1: /D11_HV_OUT_COM -> /D11_IN_COM
- C37 pad 1: /D12_HV_OUT_COM -> /D12_IN_COM
- C38 pad 2: /D12_HV_OUT_COM -> /D12_IN_COM
- C39 pad 1: /D12_HV_OUT_COM -> /D12_IN_COM
- C40 pad 1: /D13_HV_OUT_COM -> /D13_IN_COM
- C41 pad 1: Net-(C52-Pad1) -> Net-(C41-Pad1)
- C41 pad 2: /D13_HV_OUT_COM -> /D13_IN_COM
- C42 pad 1: /D13_HV_OUT_COM -> /D13_IN_COM
- C44 pad 1: Net-(C56-Pad1) -> Net-(C44-Pad1)
- C44 pad 2: /D14_HV_OUT_COM -> /D14_IN_COM
- C45 pad 1: /D14_HV_OUT_COM -> /D14_IN_COM
- C46 pad 1: /D15_HV_OUT_COM -> /D15_IN_COM
- C47 pad 1: Net-(C60-Pad1) -> Net-(C47-Pad1)
- C47 pad 2: /D15_HV_OUT_COM -> /D15_IN_COM
- C48 pad 1: /D15_HV_OUT_COM -> /D15_IN_COM
- C49 pad 1: /D16_HV_OUT_COM -> /D16_IN_COM
- C50 pad 2: /D16_HV_OUT_COM -> /D16_IN_COM
- C51 pad 1: /D16_HV_OUT_COM -> /D16_IN_COM
- C52 pad 1: /D9_HV_OUT_COM -> /D9_IN_COM
- C53 pad 1: Net-(C68-Pad1) -> Net-(C53-Pad1)
- C53 pad 2: /D9_HV_OUT_COM -> /D9_IN_COM
- C54 pad 1: /D9_HV_OUT_COM -> /D9_IN_COM
- C55 pad 1: /D14_HV_OUT_COM -> /D18_IN_COM
- C57 pad 1: /D14_HV_OUT -> /D18_IN_COM
- C57 pad 2: Net-(C57-Pad2) -> -48V
- C61 pad 1: /D15_HV_OUT -> /D20_IN_COM
- C61 pad 2: Net-(C61-Pad2) -> +48V
- C64 pad 1: /D21_HV_OUT_COM -> /D21_IN_COM
- C65 pad 1: Net-(C84-Pad1) -> Net-(C65-Pad1)
- C65 pad 2: /D21_HV_OUT_COM -> /D21_IN_COM
- C66 pad 1: /D21_HV_OUT_COM -> /D21_IN_COM
- C69 pad 1: /D9_HV_OUT -> /D22_IN_COM
- C69 pad 2: Net-(C69-Pad2) -> -48V
- C7 pad 1: /D2_HV_OUT_COM -> /D2_IN_COM
- C70 pad 1: /D23_HV_OUT_COM -> /D23_IN_COM
- C71 pad 2: /D23_HV_OUT_COM -> /D23_IN_COM
- C72 pad 1: /D23_HV_OUT_COM -> /D23_IN_COM
- C73 pad 1: /D24_HV_OUT_COM -> /D24_IN_COM
- C74 pad 2: /D24_HV_OUT_COM -> /D24_IN_COM
- C75 pad 1: /D24_HV_OUT_COM -> /D24_IN_COM
- C76 pad 1: Net-(C76-Pad1) -> /D17_IN_COM
- C76 pad 2: /D19_HV_OUT_COM -> +48V
- C77 pad 1: /D19_HV_OUT -> Net-(C77-Pad1)
- C77 pad 2: Net-(C77-Pad2) -> /D17_IN_COM
- C78 pad 1: /D19_HV_OUT_COM -> /D17_IN_COM
- C79 pad 1: /D20_HV_OUT_COM -> /D26_IN_COM
- C8 pad 2: /D2_HV_OUT_COM -> /D2_IN_COM
- C80 pad 2: /D20_HV_OUT_COM -> /D26_IN_COM
- C81 pad 1: /D20_HV_OUT -> /D26_IN_COM
- C81 pad 2: Net-(C81-Pad2) -> -48V
- C82 pad 1: /D27_HV_OUT_COM -> /D27_IN_COM
- C83 pad 2: /D27_HV_OUT_COM -> /D27_IN_COM
- C84 pad 1: /D27_HV_OUT_COM -> /D27_IN_COM
- C85 pad 1: /D28_HV_OUT_COM -> /D28_IN_COM
- C86 pad 2: /D28_HV_OUT_COM -> /D28_IN_COM
- C87 pad 1: /D28_HV_OUT_COM -> /D28_IN_COM
- C88 pad 1: /D29_HV_OUT_COM -> /D29_IN_COM
- C89 pad 2: /D29_HV_OUT_COM -> /D29_IN_COM
- C9 pad 1: /D2_HV_OUT_COM -> /D2_IN_COM
- C90 pad 1: /D29_HV_OUT_COM -> /D29_IN_COM
- C93 pad 1: /D23_HV_OUT -> /D30_IN_COM
- C93 pad 2: Net-(C93-Pad2) -> -48V
- C95 pad 2: /D31_HV_OUT_COM -> /D31_IN_COM
- C96 pad 1: /D31_HV_OUT_COM -> /D31_IN_COM
- C97 pad 1: /D32_HV_OUT_COM -> /D32_IN_COM
- C98 pad 2: /D32_HV_OUT_COM -> /D32_IN_COM
- C99 pad 1: /D32_HV_OUT_COM -> /D32_IN_COM
- FL1 pad 1: /D2_IN -> Net-(FL1-Pad1)
- FL1 pad 3: /D2_HV_OUT_COM -> /D2_IN_COM
- FL10 pad 1: /D11_IN -> Net-(FL10-Pad1)
- FL10 pad 3: /D11_HV_OUT_COM -> /D11_IN_COM
- FL11 pad 1: /D12_IN -> Net-(FL11-Pad1)
- FL11 pad 3: /D12_HV_OUT_COM -> /D12_IN_COM
- FL12 pad 1: /D13_IN -> Net-(FL12-Pad1)
- FL12 pad 3: /D13_HV_OUT_COM -> /D13_IN_COM
- FL13 pad 1: /D14_IN -> Net-(FL13-Pad1)
- FL13 pad 3: /D14_HV_OUT_COM -> /D14_IN_COM
- FL14 pad 1: /D15_IN -> Net-(FL14-Pad1)
- FL14 pad 3: /D15_HV_OUT_COM -> /D15_IN_COM
- FL15 pad 1: /D16_IN -> Net-(FL15-Pad1)
- FL15 pad 3: /D16_HV_OUT_COM -> /D16_IN_COM
- FL16 pad 1: /D9_IN -> Net-(FL16-Pad1)
- FL16 pad 3: /D9_HV_OUT_COM -> /D9_IN_COM
- FL17 pad 1: /D18_IN -> Net-(FL17-Pad1)
- FL17 pad 3: /D18_HV_OUT_COM -> /D18_IN_COM
- FL18 pad 1: /D19_IN -> Net-(FL18-Pad1)
- FL18 pad 3: /D19_HV_OUT_COM -> /D19_IN_COM
- FL19 pad 1: /D20_IN -> Net-(FL19-Pad1)
- FL19 pad 3: /D20_HV_OUT_COM -> /D20_IN_COM
- FL2 pad 1: /D3_IN -> Net-(FL2-Pad1)
- FL2 pad 3: /D3_HV_OUT_COM -> /D3_IN_COM
- FL20 pad 1: /D21_IN -> Net-(FL20-Pad1)
- FL20 pad 3: /D21_HV_OUT_COM -> /D21_IN_COM
- FL21 pad 1: /D22_IN -> Net-(FL21-Pad1)
- FL21 pad 3: /D22_HV_OUT_COM -> /D22_IN_COM
- FL22 pad 1: /D23_IN -> Net-(FL22-Pad1)
- FL22 pad 3: /D23_HV_OUT_COM -> /D23_IN_COM
- FL23 pad 1: /D24_IN -> Net-(FL23-Pad1)
- FL23 pad 3: /D24_HV_OUT_COM -> /D24_IN_COM
- FL24 pad 1: /D17_IN -> Net-(FL24-Pad1)
- FL24 pad 3: /D17_HV_OUT_COM -> /D17_IN_COM
- FL25 pad 1: /D26_IN -> Net-(FL25-Pad1)
- FL25 pad 3: /D26_HV_OUT_COM -> /D26_IN_COM
- FL26 pad 1: /D27_IN -> Net-(FL26-Pad1)
- FL26 pad 3: /D27_HV_OUT_COM -> /D27_IN_COM
- FL27 pad 1: /D28_IN -> Net-(FL27-Pad1)
- FL27 pad 3: /D28_HV_OUT_COM -> /D28_IN_COM
- FL28 pad 1: /D29_IN -> Net-(FL28-Pad1)
- FL28 pad 3: /D29_HV_OUT_COM -> /D29_IN_COM
- FL29 pad 1: /D30_IN -> Net-(FL29-Pad1)
- FL29 pad 3: /D30_HV_OUT_COM -> /D30_IN_COM
- FL3 pad 1: /D4_IN -> Net-(FL3-Pad1)
- FL3 pad 3: /D4_HV_OUT_COM -> /D4_IN_COM
- FL30 pad 1: /D31_IN -> Net-(FL30-Pad1)
- FL30 pad 3: /D31_HV_OUT_COM -> /D31_IN_COM
- FL31 pad 1: /D32_IN -> Net-(FL31-Pad1)
- FL31 pad 3: /D32_HV_OUT_COM -> /D32_IN_COM
- FL32 pad 1: /D25_IN -> Net-(FL32-Pad1)
- FL32 pad 3: /D25_HV_OUT_COM -> /D25_IN_COM
- FL4 pad 1: /D5_IN -> Net-(FL4-Pad1)
- FL4 pad 3: /D5_HV_OUT_COM -> /D5_IN_COM
- FL5 pad 1: /D6_IN -> Net-(FL5-Pad1)
- FL5 pad 3: /D6_HV_OUT_COM -> /D6_IN_COM
- FL6 pad 1: /D7_IN -> Net-(FL6-Pad1)
- FL6 pad 3: /D7_HV_OUT_COM -> /D7_IN_COM
- FL7 pad 1: /D8_IN -> Net-(FL7-Pad1)
- FL7 pad 3: /D8_HV_OUT_COM -> /D8_IN_COM
- FL8 pad 1: /D1_IN -> Net-(FL8-Pad1)
- FL8 pad 3: /D1_HV_OUT_COM -> /D1_IN_COM
- FL9 pad 1: /D10_IN -> Net-(FL9-Pad1)
- FL9 pad 3: /D10_HV_OUT_COM -> /D10_IN_COM
- J2 pad 35: /D1_HV_OUT_COM -> /D1_IN_COM
- J2 pad 36: /D2_HV_OUT_COM -> /D2_IN_COM
- J2 pad 37: /D3_HV_OUT_COM -> /D3_IN_COM
- J2 pad 38: /D4_HV_OUT_COM -> /D4_IN_COM
- J2 pad 39: /D5_HV_OUT_COM -> /D5_IN_COM
- J2 pad 40: /D6_HV_OUT_COM -> /D6_IN_COM
- J2 pad 41: /D7_HV_OUT_COM -> /D7_IN_COM
- J2 pad 42: /D8_HV_OUT_COM -> /D8_IN_COM
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
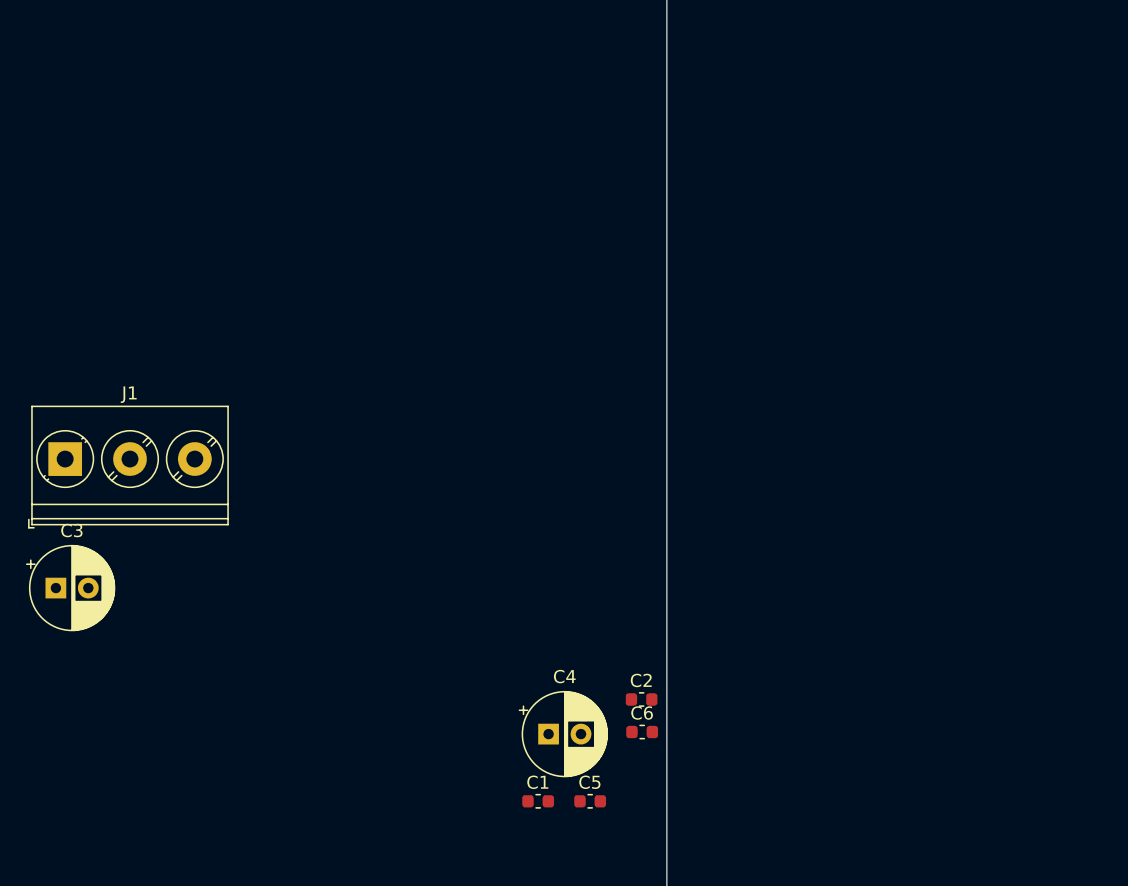
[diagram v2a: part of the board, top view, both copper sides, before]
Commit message: Small edit to position of some components
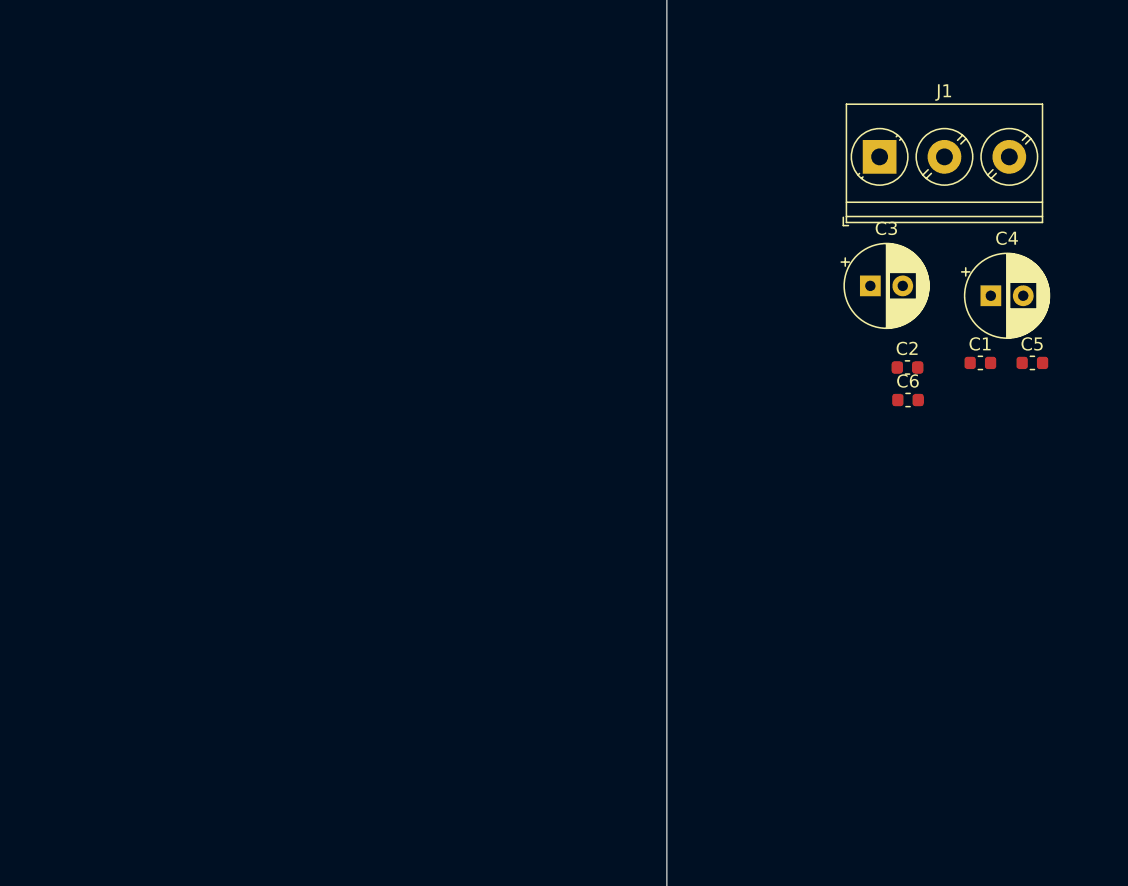
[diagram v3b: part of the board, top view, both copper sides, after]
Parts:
- moved C3 67.0 mm to (118.6, 219.7)
- moved J1 67.0 mm to (119.3, 209.8)
- moved C5 48.0 mm to (131.1, 225.7)
- moved C1 48.0 mm to (127.0, 225.7)
- moved C4 48.0 mm to (127.9, 220.5)
- moved C2 32.8 mm to (121.4, 226.0)
- moved C6 32.8 mm to (121.5, 228.5)

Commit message: Updating with recent changes as layout work starts
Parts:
- C100, C101, C102, C55, C56, C57, C58, C59, C60, C61, C62, C63, C64, C65, C66, C67, C68, C69, C70, C71, C72, C73, C74, C75, C76, C77, C78, C79, C80, C81, C82, C83, C84, C85, C86, C87, C88, C89, C90, C91, C92, C93, C94, C95, C96, C97, C98, C99, FL17, FL18, FL19, FL20, FL21, FL22, FL23, FL24, FL25, FL26, FL27, FL28, FL29, FL30, FL31, FL32, IC17, IC18, IC19, IC20, IC21, IC22, IC23, IC24, IC25, IC26, IC27, IC28, IC29, IC30, IC31, IC32, L17, L18, L19, L20, L21, L22, L23, L24, L25, L26, L27, L28, L29, L30, L31, L32, R100, R101, R102, R103, R104, R105, R106, R107, R108, R109, R110, R111, R112, R113, R114, R115, R116, R117, R118, R119, R120, R121, R122, R123, R124, R125, R126, R127, R128, R129, R130, R131, R132, R133, R134, R135, R136, R137, R138, R139, R140, R141, R142, R143, R144, R145, R146, R147, R148, R149, R150, R151, R152, R153, R154, R155, R156, R157, R158, R159, R160, R161, R162, R163, R164, R165, R166, R167, R168, R169, R170, R171, R172, R173, R174, R175, R176, R177, R178, R179, R180, R181, R182, R183, R184, R185, R186, R187, R188, R189, R190, R191, R192, R97, R98, R99: moved to B.Cu
- moved L8 297.5 mm to (137.3, 171.3), turned to 90 degrees
- moved C28 297.4 mm to (138.1, 181.6)
- moved C29 297.4 mm to (128.9, 184.0)
- moved R45 297.4 mm to (128.9, 180.9)
- moved C30 297.4 mm to (135.7, 184.5)
- moved IC8 297.4 mm to (133.5, 180.9)
- moved R44 297.4 mm to (126.5, 181.9)
- moved R47 297.4 mm to (133.5, 177.3)
- moved R48 297.4 mm to (126.5, 180.3)
- moved R46 297.2 mm to (139.7, 180.8), turned to 270 degrees
- moved FL8 295.6 mm to (127.7, 191.1)
- moved R43 295.6 mm to (131.2, 195.5)
- moved L32 275.6 mm to (149.2, 247.0)
- moved R191 275.4 mm to (145.4, 241.0)
- moved R192 273.5 mm to (138.4, 238.0)
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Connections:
- L1 pad 1: Net-(L1-Pad1) -> /D2_IN_COM
- L1 pad 2: /D2_IN_COM -> Net-(L1-Pad2)
- L1 pad 3: /D2_HV_OUT_COM -> /D2_HV_OUT
- L1 pad 4: /D2_HV_OUT -> /D2_HV_OUT_COM
- L2 pad 1: Net-(L2-Pad1) -> /D3_IN_COM
- L2 pad 2: /D3_IN_COM -> Net-(L2-Pad2)
- L2 pad 3: /D3_HV_OUT_COM -> /D3_HV_OUT
- L2 pad 4: /D3_HV_OUT -> /D3_HV_OUT_COM
- L25 pad 1: Net-(L25-Pad1) -> /D26_IN_COM
- L25 pad 2: /D26_IN_COM -> Net-(L25-Pad2)
- L25 pad 3: /D26_HV_OUT_COM -> /D26_HV_OUT
- L25 pad 4: /D26_HV_OUT -> /D26_HV_OUT_COM
- L26 pad 1: Net-(L26-Pad1) -> /D27_IN_COM
- L26 pad 2: /D27_IN_COM -> Net-(L26-Pad2)
- L26 pad 3: /D27_HV_OUT_COM -> /D27_HV_OUT
- L26 pad 4: /D27_HV_OUT -> /D27_HV_OUT_COM
- L27 pad 1: Net-(L27-Pad1) -> /D28_IN_COM
- L27 pad 2: /D28_IN_COM -> Net-(L27-Pad2)
- L27 pad 3: /D28_HV_OUT_COM -> /D28_HV_OUT
- L27 pad 4: /D28_HV_OUT -> /D28_HV_OUT_COM
- L28 pad 1: Net-(L28-Pad1) -> /D29_IN_COM
- L28 pad 2: /D29_IN_COM -> Net-(L28-Pad2)
- L28 pad 3: /D29_HV_OUT_COM -> /D29_HV_OUT
- L28 pad 4: /D29_HV_OUT -> /D29_HV_OUT_COM
- L29 pad 1: Net-(L29-Pad1) -> /D30_IN_COM
- L29 pad 2: /D30_IN_COM -> Net-(L29-Pad2)
- L29 pad 3: /D30_HV_OUT_COM -> /D30_HV_OUT
- L29 pad 4: /D30_HV_OUT -> /D30_HV_OUT_COM
- L3 pad 1: Net-(L3-Pad1) -> /D4_IN_COM
- L3 pad 2: /D4_IN_COM -> Net-(L3-Pad2)
- L3 pad 3: /D4_HV_OUT_COM -> /D4_HV_OUT
- L3 pad 4: /D4_HV_OUT -> /D4_HV_OUT_COM
- L30 pad 1: Net-(L30-Pad1) -> /D31_IN_COM
- L30 pad 2: /D31_IN_COM -> Net-(L30-Pad2)
- L30 pad 3: /D31_HV_OUT_COM -> /D31_HV_OUT
- L30 pad 4: /D31_HV_OUT -> /D31_HV_OUT_COM
- L31 pad 1: Net-(L31-Pad1) -> /D32_IN_COM
- L31 pad 2: /D32_IN_COM -> Net-(L31-Pad2)
- L31 pad 3: /D32_HV_OUT_COM -> /D32_HV_OUT
- L31 pad 4: /D32_HV_OUT -> /D32_HV_OUT_COM
- L32 pad 1: Net-(L32-Pad1) -> /D25_IN_COM
- L32 pad 2: /D25_IN_COM -> Net-(L32-Pad2)
- L32 pad 3: /D25_HV_OUT_COM -> /D25_HV_OUT
- L32 pad 4: /D25_HV_OUT -> /D25_HV_OUT_COM
- L4 pad 1: Net-(L4-Pad1) -> /D5_IN_COM
- L4 pad 2: /D5_IN_COM -> Net-(L4-Pad2)
- L4 pad 3: /D5_HV_OUT_COM -> /D5_HV_OUT
- L4 pad 4: /D5_HV_OUT -> /D5_HV_OUT_COM
- L5 pad 1: Net-(L5-Pad1) -> /D6_IN_COM
- L5 pad 2: /D6_IN_COM -> Net-(L5-Pad2)
- L5 pad 3: /D6_HV_OUT_COM -> /D6_HV_OUT
- L5 pad 4: /D6_HV_OUT -> /D6_HV_OUT_COM
- L6 pad 1: Net-(L6-Pad1) -> /D7_IN_COM
- L6 pad 2: /D7_IN_COM -> Net-(L6-Pad2)
- L6 pad 3: /D7_HV_OUT_COM -> /D7_HV_OUT
- L6 pad 4: /D7_HV_OUT -> /D7_HV_OUT_COM
- L7 pad 1: Net-(L7-Pad1) -> /D8_IN_COM
- L7 pad 2: /D8_IN_COM -> Net-(L7-Pad2)
- L7 pad 3: /D8_HV_OUT_COM -> /D8_HV_OUT
- L7 pad 4: /D8_HV_OUT -> /D8_HV_OUT_COM
- L8 pad 1: Net-(L8-Pad1) -> /D1_IN_COM
- L8 pad 2: /D1_IN_COM -> Net-(L8-Pad2)
- L8 pad 3: /D1_HV_OUT_COM -> /D1_HV_OUT
- L8 pad 4: /D1_HV_OUT -> /D1_HV_OUT_COM
- R10 pad 1: Net-(L2-Pad1) -> Net-(L2-Pad2)
- R148 pad 1: Net-(L25-Pad1) -> Net-(L25-Pad2)
- R154 pad 1: Net-(L26-Pad1) -> Net-(L26-Pad2)
- R16 pad 1: Net-(L3-Pad1) -> Net-(L3-Pad2)
- R160 pad 1: Net-(L27-Pad1) -> Net-(L27-Pad2)
- R166 pad 1: Net-(L28-Pad1) -> Net-(L28-Pad2)
- R172 pad 1: Net-(L29-Pad1) -> Net-(L29-Pad2)
- R178 pad 1: Net-(L30-Pad1) -> Net-(L30-Pad2)
- R184 pad 1: Net-(L31-Pad1) -> Net-(L31-Pad2)
- R190 pad 1: Net-(L32-Pad1) -> Net-(L32-Pad2)
- R22 pad 1: Net-(L4-Pad1) -> Net-(L4-Pad2)
- R28 pad 1: Net-(L5-Pad1) -> Net-(L5-Pad2)
- R34 pad 1: Net-(L6-Pad1) -> Net-(L6-Pad2)
- R4 pad 1: Net-(L1-Pad1) -> Net-(L1-Pad2)
- R40 pad 1: Net-(L7-Pad1) -> Net-(L7-Pad2)
- R46 pad 1: Net-(L8-Pad1) -> Net-(L8-Pad2)
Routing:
- net -48V: track 0.00 -> 127.1 mm
- net Net-(IC16-Pad6): track 0.00 -> 9.10 mm
- net Net-(IC9-Pad6): track 0.00 -> 5.43 mm
- added copper zone on In4.Cu, net -48V
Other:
- board size 380 x 160 mm -> 191 x 152.4 mm
- net class Default: clearance 0.2 -> 0.127; trace_width 0.25 -> 0.127; via_dia 0.8 -> 0.508; via_drill 0.4 -> 0.254
- net class Power added: clearance 0.127, trace_width 0.5, via_dia 0.8, via_drill 0.4
- rule trace_clearance: 0.2 -> 0.127
- rule trace_min: 0.2 -> 0.127
- rule via_min_drill: 0.3 -> 0.254
- rule via_min_size: 0.4 -> 0.508
